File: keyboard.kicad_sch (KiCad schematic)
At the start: 132 parts, among them SW1 SW_Push, SW10 SW_Push, SW11 SW_Push, SW12 SW_Push, SW13 SW_Push, SW14 SW_Push, SW15 SW_Push, SW16 SW_Push, SW17 SW_Push, SW18 SW_Push, SW19 SW_Push, SW2 SW_Push, SW20 SW_Push, SW21 SW_Push, SW22 SW_Push, SW23 SW_Push, SW24 SW_Push, SW25 SW_Push, SW26 SW_Push, SW27 SW_Push, SW28 SW_Push, SW29 SW_Push, SW3 SW_Push, SW30 SW_Push, SW31 SW_Push, SW32 SW_Push, SW33 SW_Push, SW34 SW_Push, SW35 SW_Push, SW36 SW_Push, SW37 SW_Push, SW38 SW_Push, SW39 SW_Push, SW4 SW_Push, SW40 SW_Push, SW41 SW_Push, SW42 SW_Push, SW43 SW_Push, SW44 SW_Push, SW45 SW_Push, SW46 SW_Push, SW47 SW_Push, SW48 SW_Push, SW49 SW_Push, SW5 SW_Push, SW50 SW_Push, SW51 SW_Push, SW52 SW_Push, SW53 SW_Push, SW54 SW_Push, SW55 SW_Push, SW56 SW_Push, SW57 SW_Push, SW58 SW_Push, SW59 SW_Push, SW6 SW_Push, SW60 SW_Push, SW61 SW_Push, SW62 SW_Push, SW63 SW_Push, SW64 SW_Push, SW7 SW_Push, SW8 SW_Push, SW9 SW_Push, U1 Pro Micro, U2 TRRS, U3 Pro Micro, U4 TRRS

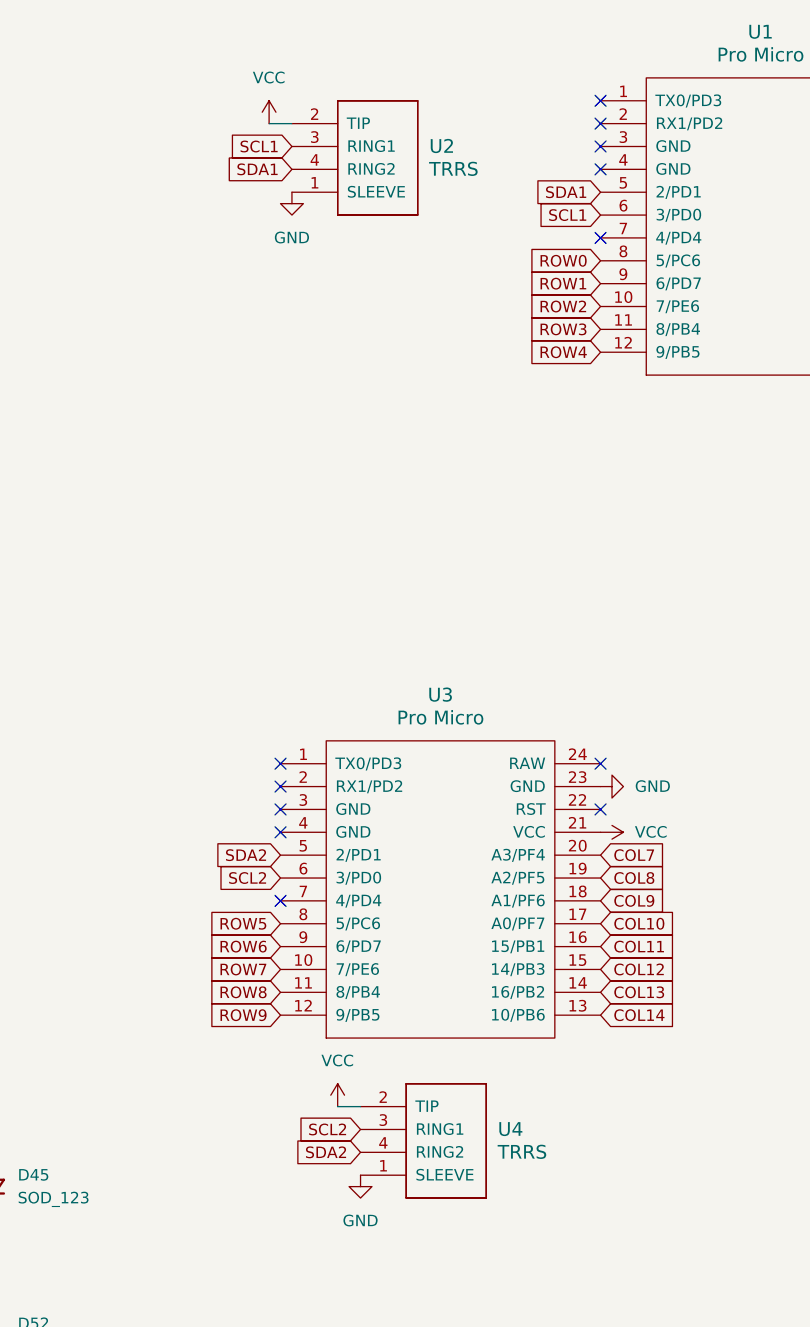
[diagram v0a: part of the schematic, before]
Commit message: Remove second connection from TRRS and ProMicro, redo traces on PCB to be cleaner
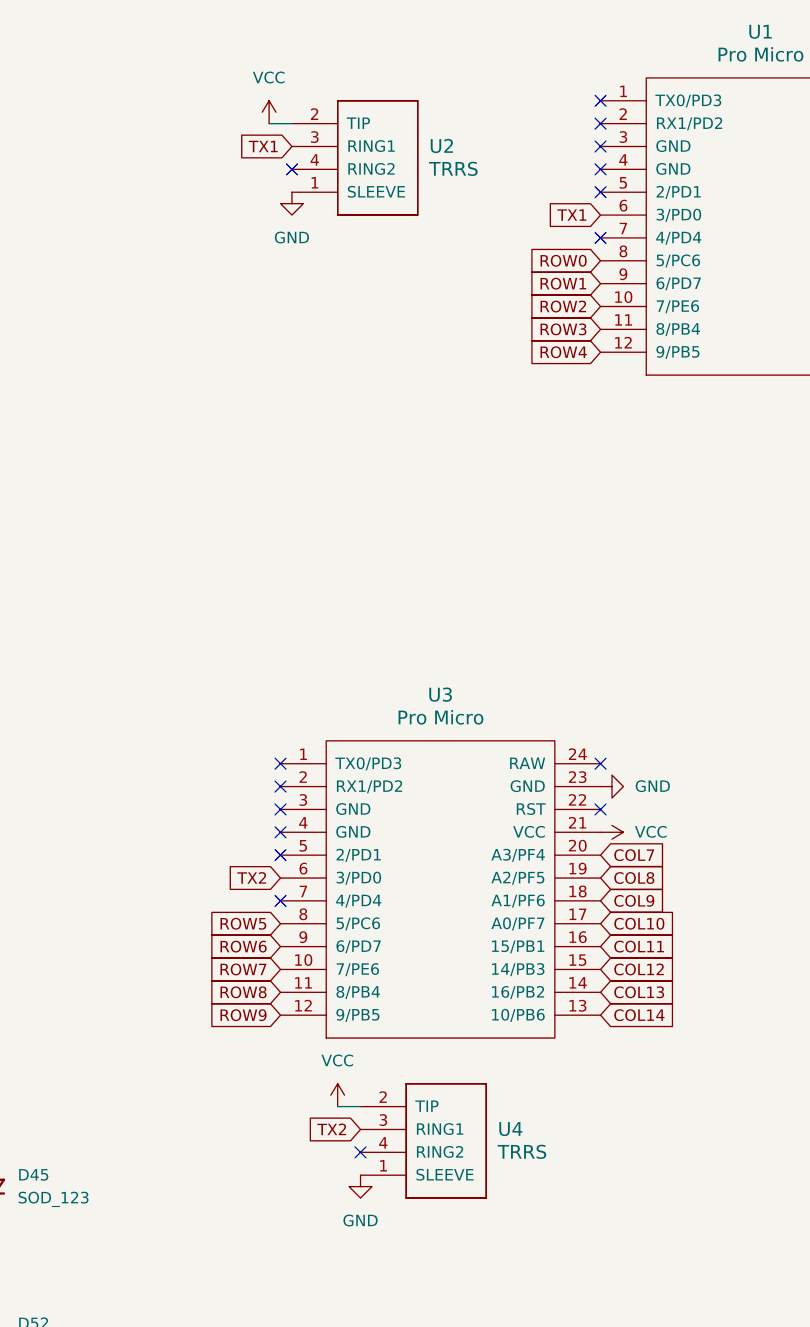
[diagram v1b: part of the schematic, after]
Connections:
- net SCL1 renamed TX1
- net SCL2 renamed TX2
- net SDA1: no longer names the net of U1.5 (2/PD1)
- net SDA1: no longer U2.4 (RING2)
- net SDA2: no longer names the net of U4.4 (RING2)
- net SDA2: no longer U3.5 (2/PD1)
- no-connect marks 15 -> 19
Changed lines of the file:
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@@
   )
   (no_connect (at 213.36 25.4))
+  (no_connect (at 177.8 104.14))
   (no_connect (at 213.36 22.86))
   (no_connect (at 213.36 35.56))
@@
   (no_connect (at 213.36 27.94))
   (no_connect (at 248.92 25.4))
+  (no_connect (at 179.07 27.94))
   (no_connect (at 213.36 99.06))
   (no_connect (at 248.92 20.32))
   (no_connect (at 177.8 99.06))
+  (no_connect (at 186.69 137.16))
+  (no_connect (at 213.36 30.48))
   (no_connect (at 248.92 48.26))
   (no_connect (at 177.8 109.22))
@@
     )
   )
-  (global_label "SDA1" (shape input) (at 213.36 30.48 180) (fields_autoplaced)
-    (effects (font (size 1.27 1.27)) (justify right))
-    (property "Intersheetrefs" "${INTERSHEET_REFS}" (at 205.5972 30.48 0)
-      (effects (font (size 1.27 1.27)) (justify right) hide)
-    )
-  )
   (global_label "ROW3" (shape input) (at 213.36 45.72 180) (fields_autoplaced)
     (effects (font (size 1.27 1.27)) (justify right))
@@
     )
   )
-  (global_label "SCL2" (shape input) (at 177.8 106.68 180) (fields_autoplaced)
-    (effects (font (size 1.27 1.27)) (justify right))
-    (property "Intersheetrefs" "${INTERSHEET_REFS}" (at 170.0977 106.68 0)
+  (global_label "TX2" (shape input) (at 177.8 106.68 180) (fields_autoplaced)
+    (effects (font (size 1.27 1.27)) (justify right))
+    (property "Intersheetrefs" "${INTERSHEET_REFS}" (at 171.4282 106.68 0)
       (effects (font (size 1.27 1.27)) (justify right) hide)
     )
@@
     )
   )
-  (global_label "SDA2" (shape input) (at 177.8 104.14 180) (fields_autoplaced)
-    (effects (font (size 1.27 1.27)) (justify right))
-    (property "Intersheetrefs" "${INTERSHEET_REFS}" (at 170.0372 104.14 0)
-      (effects (font (size 1.27 1.27)) (justify right) hide)
-    )
-  )
   (global_label "COL2" (shape input) (at 57.15 21.59 90) (fields_autoplaced)
     (effects (font (size 1.27 1.27)) (justify left))
@@
     )
   )
-  (global_label "SCL1" (shape input) (at 213.36 33.02 180) (fields_autoplaced)
-    (effects (font (size 1.27 1.27)) (justify right))
-    (property "Intersheetrefs" "${INTERSHEET_REFS}" (at 205.6577 33.02 0)
+  (global_label "TX1" (shape input) (at 213.36 33.02 180) (fields_autoplaced)
+    (effects (font (size 1.27 1.27)) (justify right))
+    (property "Intersheetrefs" "${INTERSHEET_REFS}" (at 206.9882 33.02 0)
       (effects (font (size 1.27 1.27)) (justify right) hide)
     )
@@
     )
   )
-  (global_label "SCL1" (shape input) (at 179.07 25.4 180) (fields_autoplaced)
-    (effects (font (size 1.27 1.27)) (justify right))
-    (property "Intersheetrefs" "${INTERSHEET_REFS}" (at 171.3677 25.4 0)
-      (effects (font (size 1.27 1.27)) (justify right) hide)
-    )
-  )
-  (global_label "SDA1" (shape input) (at 179.07 27.94 180) (fields_autoplaced)
-    (effects (font (size 1.27 1.27)) (justify right))
-    (property "Intersheetrefs" "${INTERSHEET_REFS}" (at 171.3072 27.94 0)
+  (global_label "TX1" (shape input) (at 179.07 25.4 180) (fields_autoplaced)
+    (effects (font (size 1.27 1.27)) (justify right))
+    (property "Intersheetrefs" "${INTERSHEET_REFS}" (at 172.6982 25.4 0)
       (effects (font (size 1.27 1.27)) (justify right) hide)
     )
@@
     )
   )
-  (global_label "SCL2" (shape input) (at 186.69 134.62 180) (fields_autoplaced)
-    (effects (font (size 1.27 1.27)) (justify right))
-    (property "Intersheetrefs" "${INTERSHEET_REFS}" (at 178.9877 134.62 0)
+  (global_label "TX2" (shape input) (at 186.69 134.62 180) (fields_autoplaced)
+    (effects (font (size 1.27 1.27)) (justify right))
+    (property "Intersheetrefs" "${INTERSHEET_REFS}" (at 180.3182 134.62 0)
       (effects (font (size 1.27 1.27)) (justify right) hide)
     )
@@
       (effects (font (size 1.27 1.27)) (justify right) hide)
     )
-  )
-  (global_label "SDA2" (shape input) (at 186.69 137.16 180) (fields_autoplaced)
-    (effects (font (size 1.27 1.27)) (justify right))
-    (property "Intersheetrefs" "${INTERSHEET_REFS}" (at 178.9272 137.16 0)
-      (effects (font (size 1.27 1.27)) (justify right) hide)
-    )

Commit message: Add JLCPCB part numbers
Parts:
- D1, D10, D11, D12, D13, D14, D15, D16, D17, D18, D19, D2, D20, D21, D22, D23, D24, D25, D26, D27, D28, D29, D3, D30, D31, D32, D33, D34, D35, D36, D37, D38, D39, D4, D40, D41, D42, D43, D44, D45, D46, D47, D48, D49, D5, D50, D51, D52, D53, D54, D55, D56, D57, D58, D59, D6, D60, D61, D62, D63, D64, D7, D8, D9: JLCPCB Part # (none) -> C258181
- U1, U3: now left out of the parts list
- U2, U4: JLCPCB Part # (none) -> C2884926

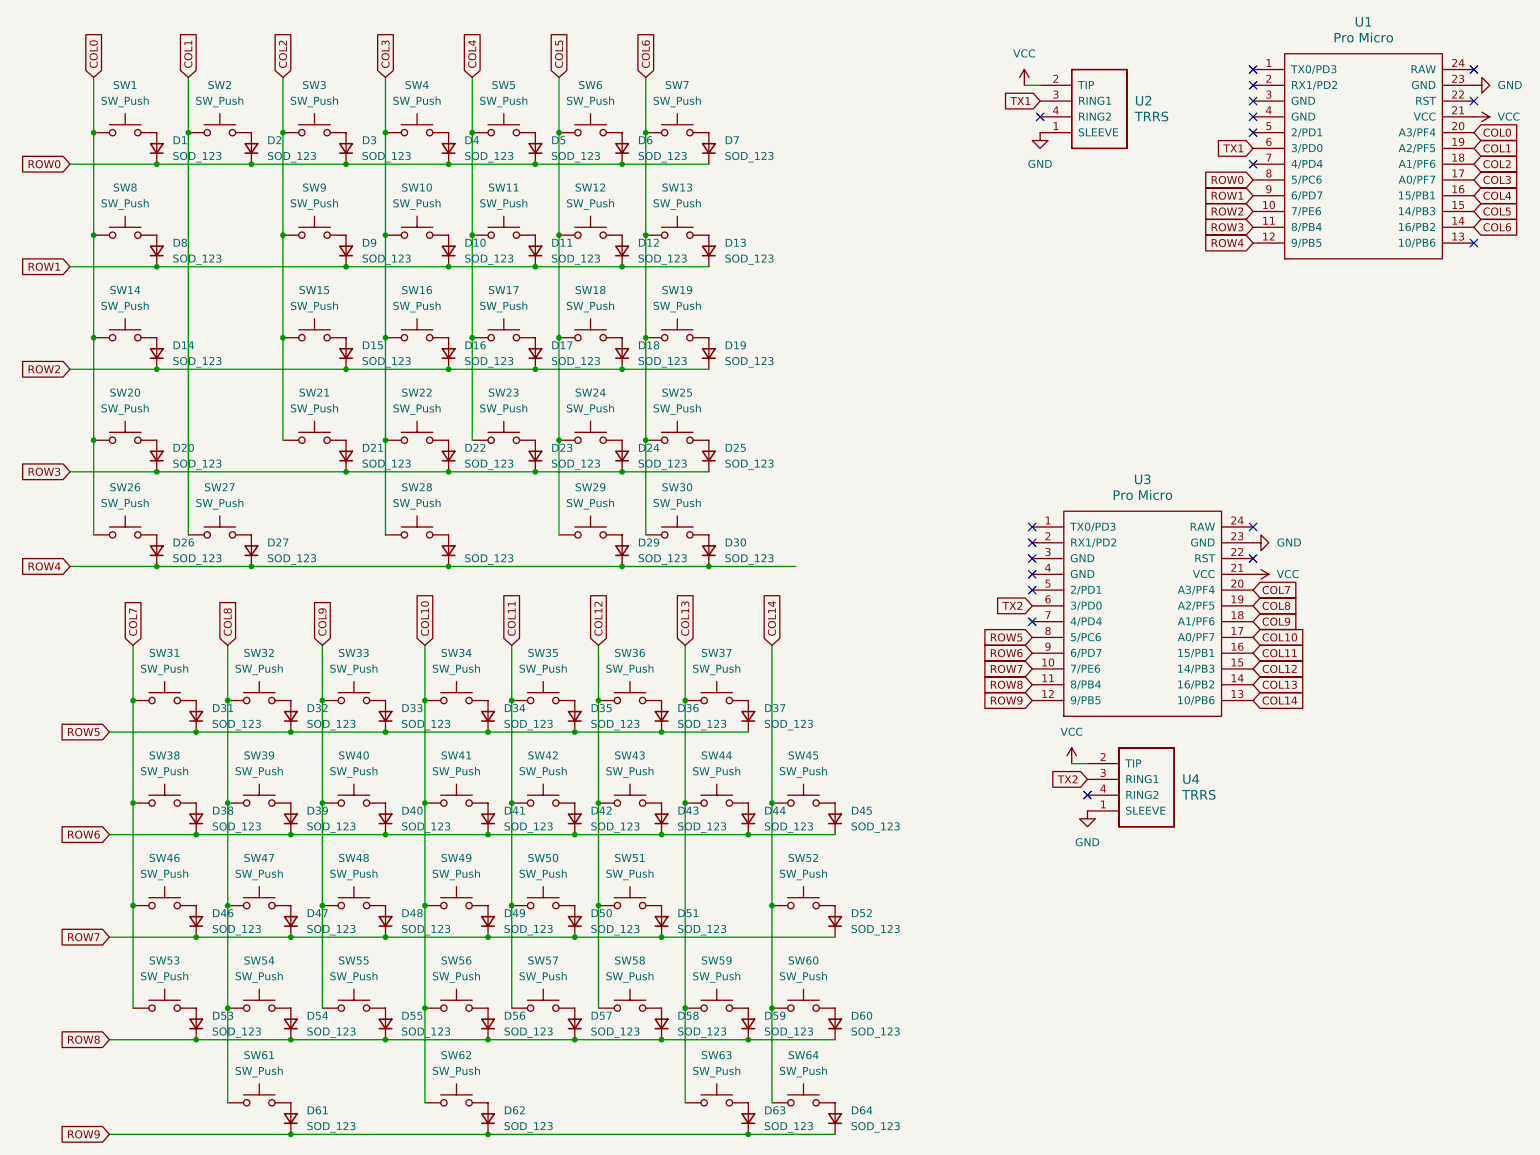
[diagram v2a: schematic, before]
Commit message: Update Diode names
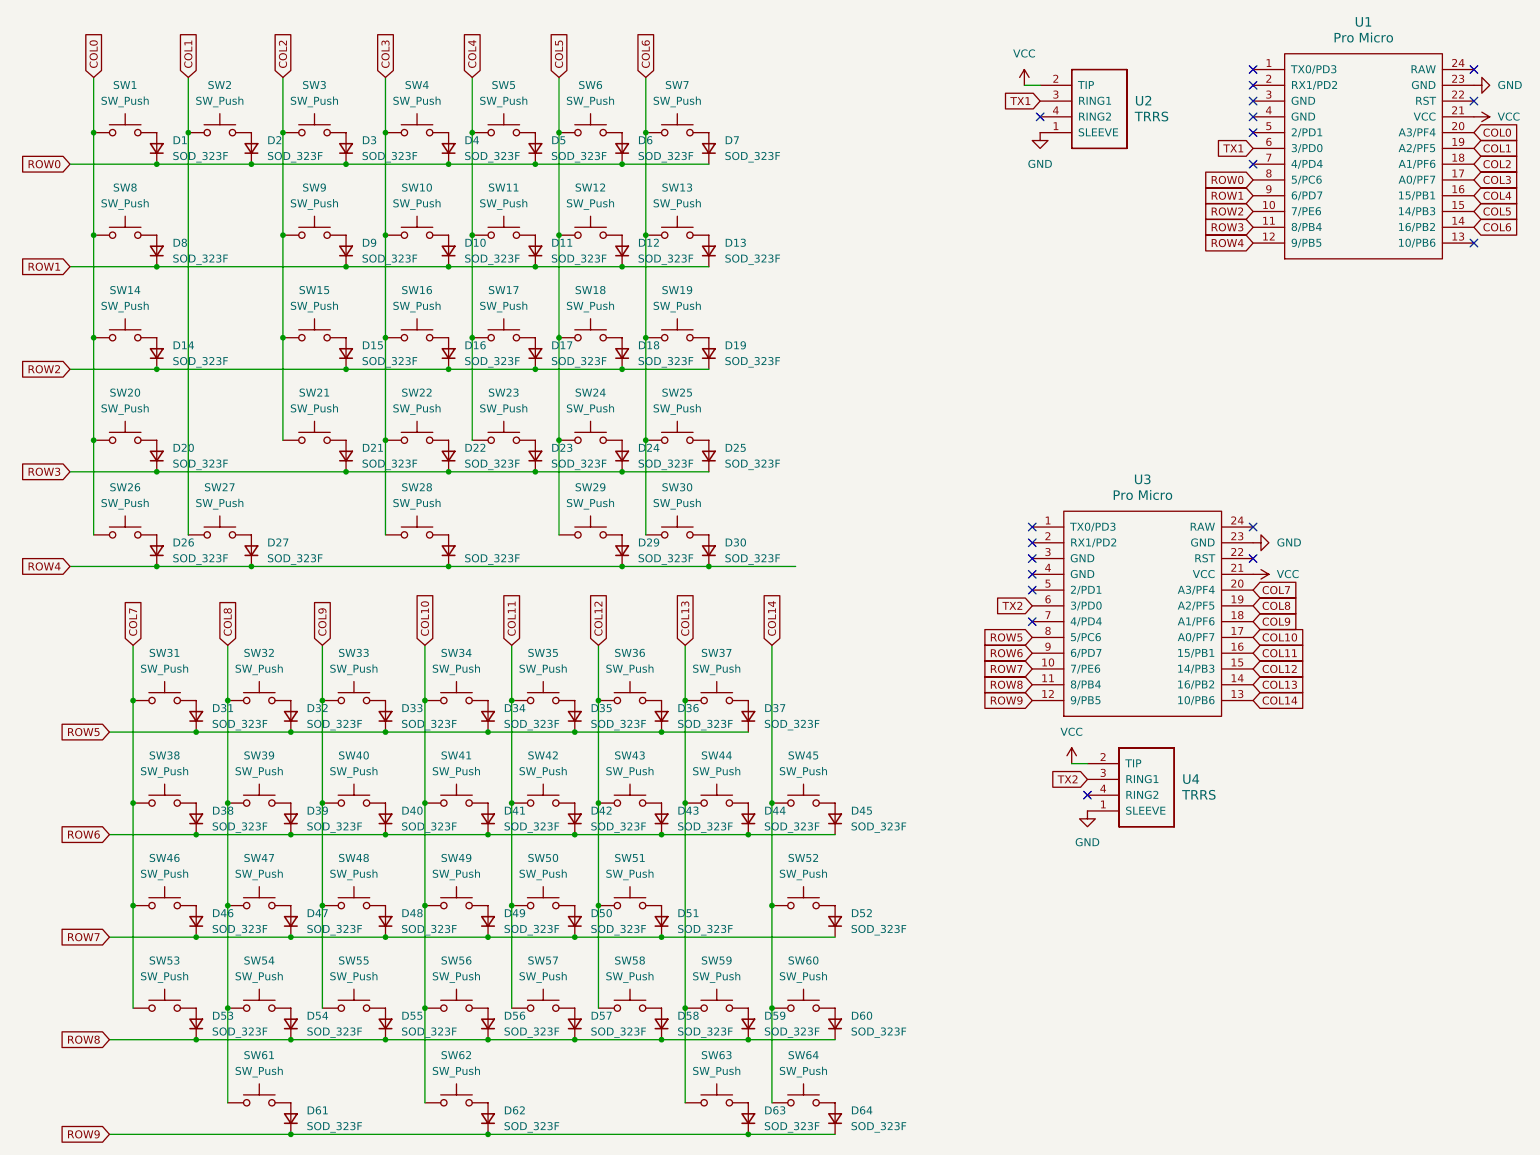
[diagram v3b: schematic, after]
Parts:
- D1, D10, D11, D12, D13, D14, D15, D16, D17, D18, D19, D2, D20, D21, D22, D23, D24, D25, D26, D27, D28, D29, D3, D30, D31, D32, D33, D34, D35, D36, D37, D38, D39, D4, D40, D41, D42, D43, D44, D45, D46, D47, D48, D49, D5, D50, D51, D52, D53, D54, D55, D56, D57, D58, D59, D6, D60, D61, D62, D63, D64, D7, D8, D9: value SOD_123 -> SOD_323F

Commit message: Change from SOD_323F to SOD_123 footprint for diodes
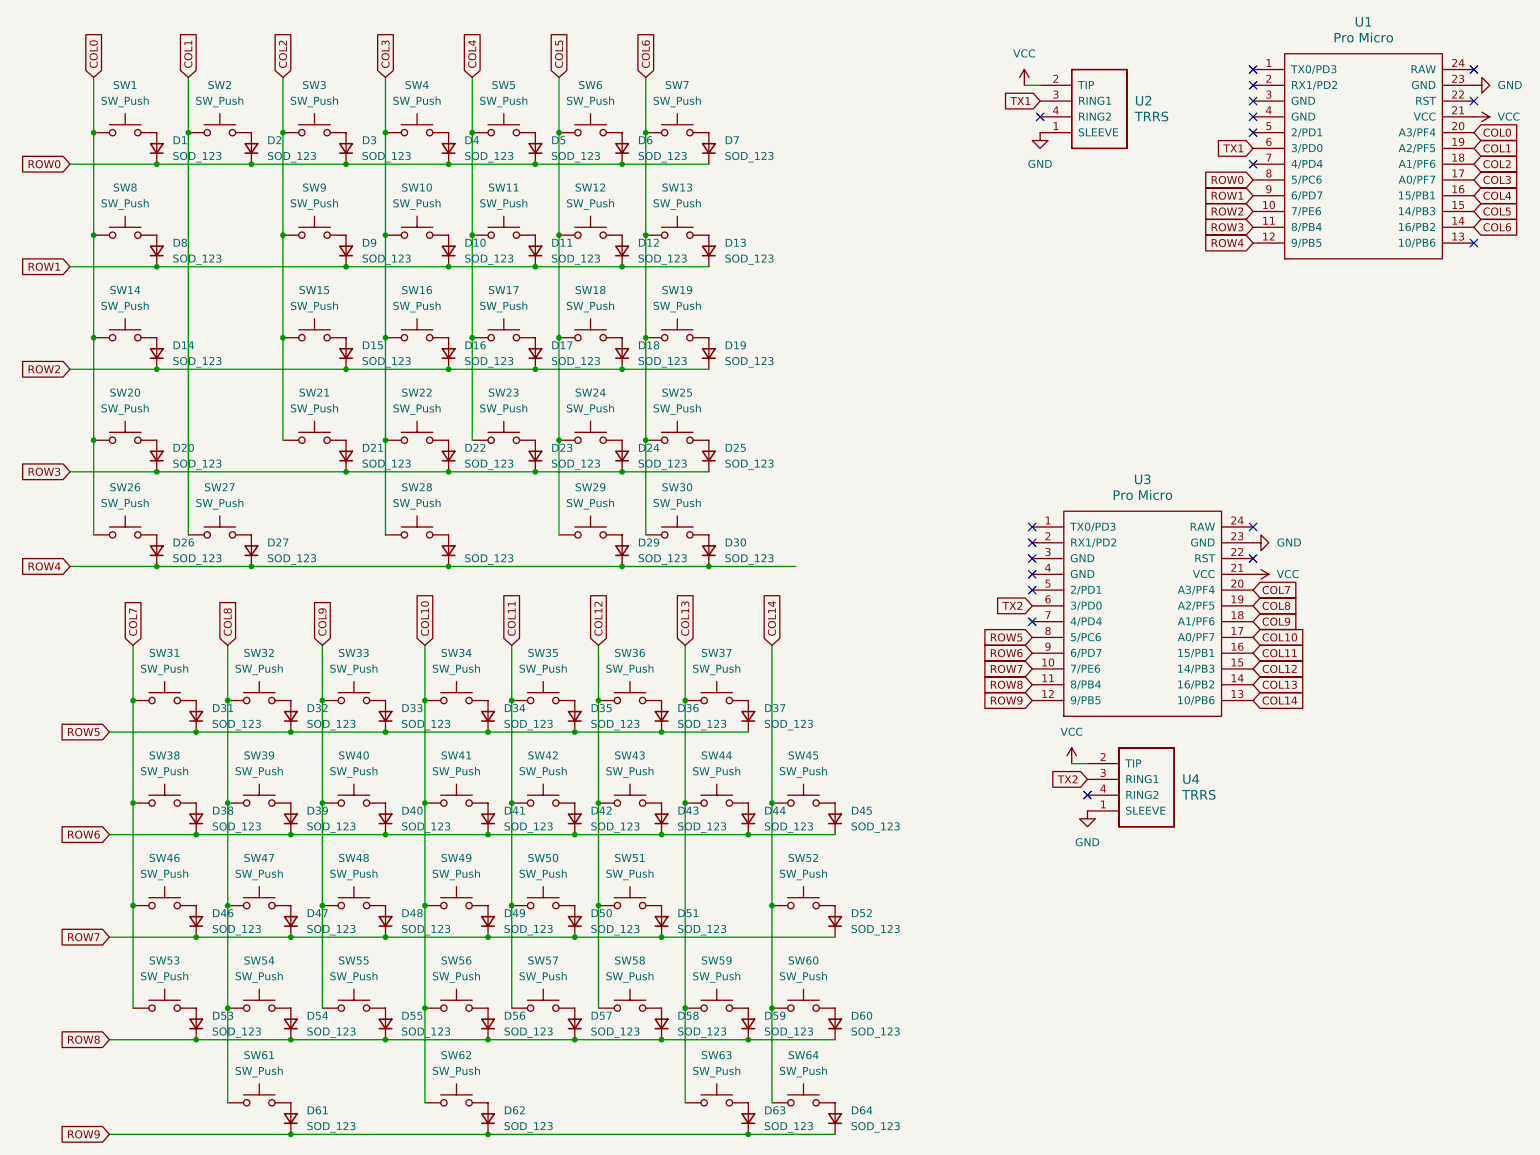
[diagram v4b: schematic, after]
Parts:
- D1, D10, D11, D12, D13, D14, D15, D16, D17, D18, D19, D2, D20, D21, D22, D23, D24, D25, D26, D27, D28, D29, D3, D30, D31, D32, D33, D34, D35, D36, D37, D38, D39, D4, D40, D41, D42, D43, D44, D45, D46, D47, D48, D49, D5, D50, D51, D52, D53, D54, D55, D56, D57, D58, D59, D6, D60, D61, D62, D63, D64, D7, D8, D9: value SOD_323F -> SOD_123; footprint Diode_SMD:D_SOD-323F -> Diode_SMD:D_SOD-123; MPN (none) -> 1N914BWS
- U2, U4: MPN (none) -> PJ-320A
